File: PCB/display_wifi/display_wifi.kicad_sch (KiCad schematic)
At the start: 17 parts, among them J1 Conn_01x02, J2 Conn_01x10, SW1 SW_Push, SW2 SW_Push, SW3 SW_Push, U1 NINA-W132, U2 OPT4001DNPRQ1

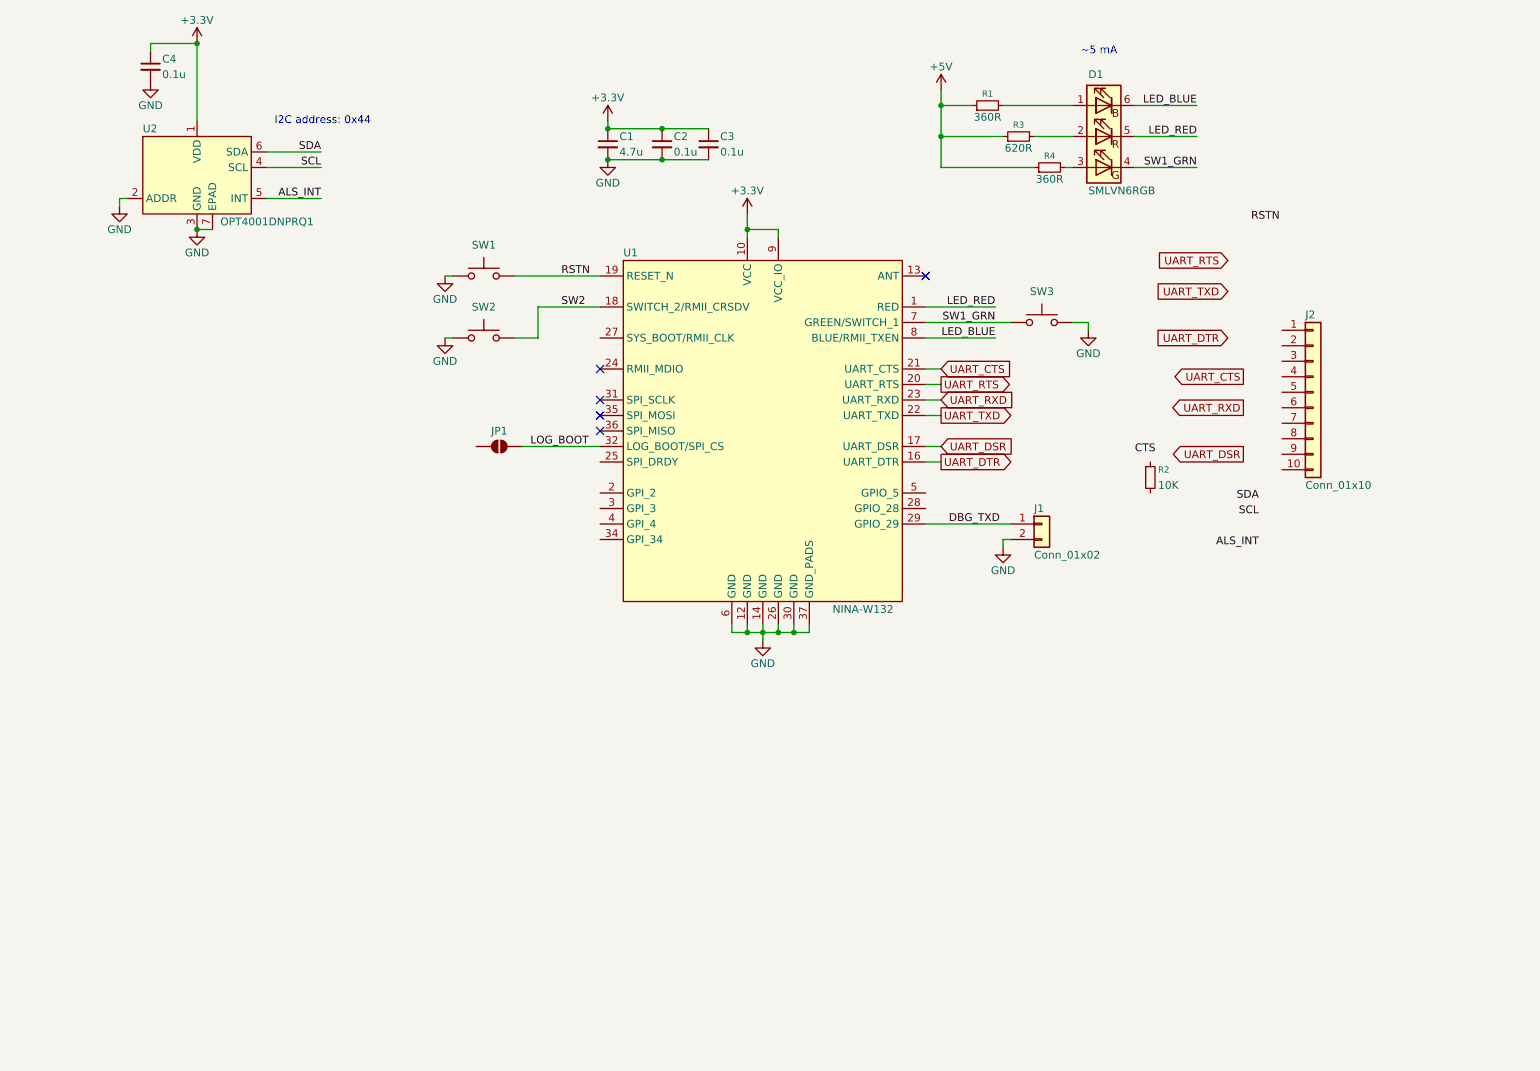
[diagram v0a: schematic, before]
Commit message: Added light sensor, IR remote sensor, test connectors, and routed PCB for display
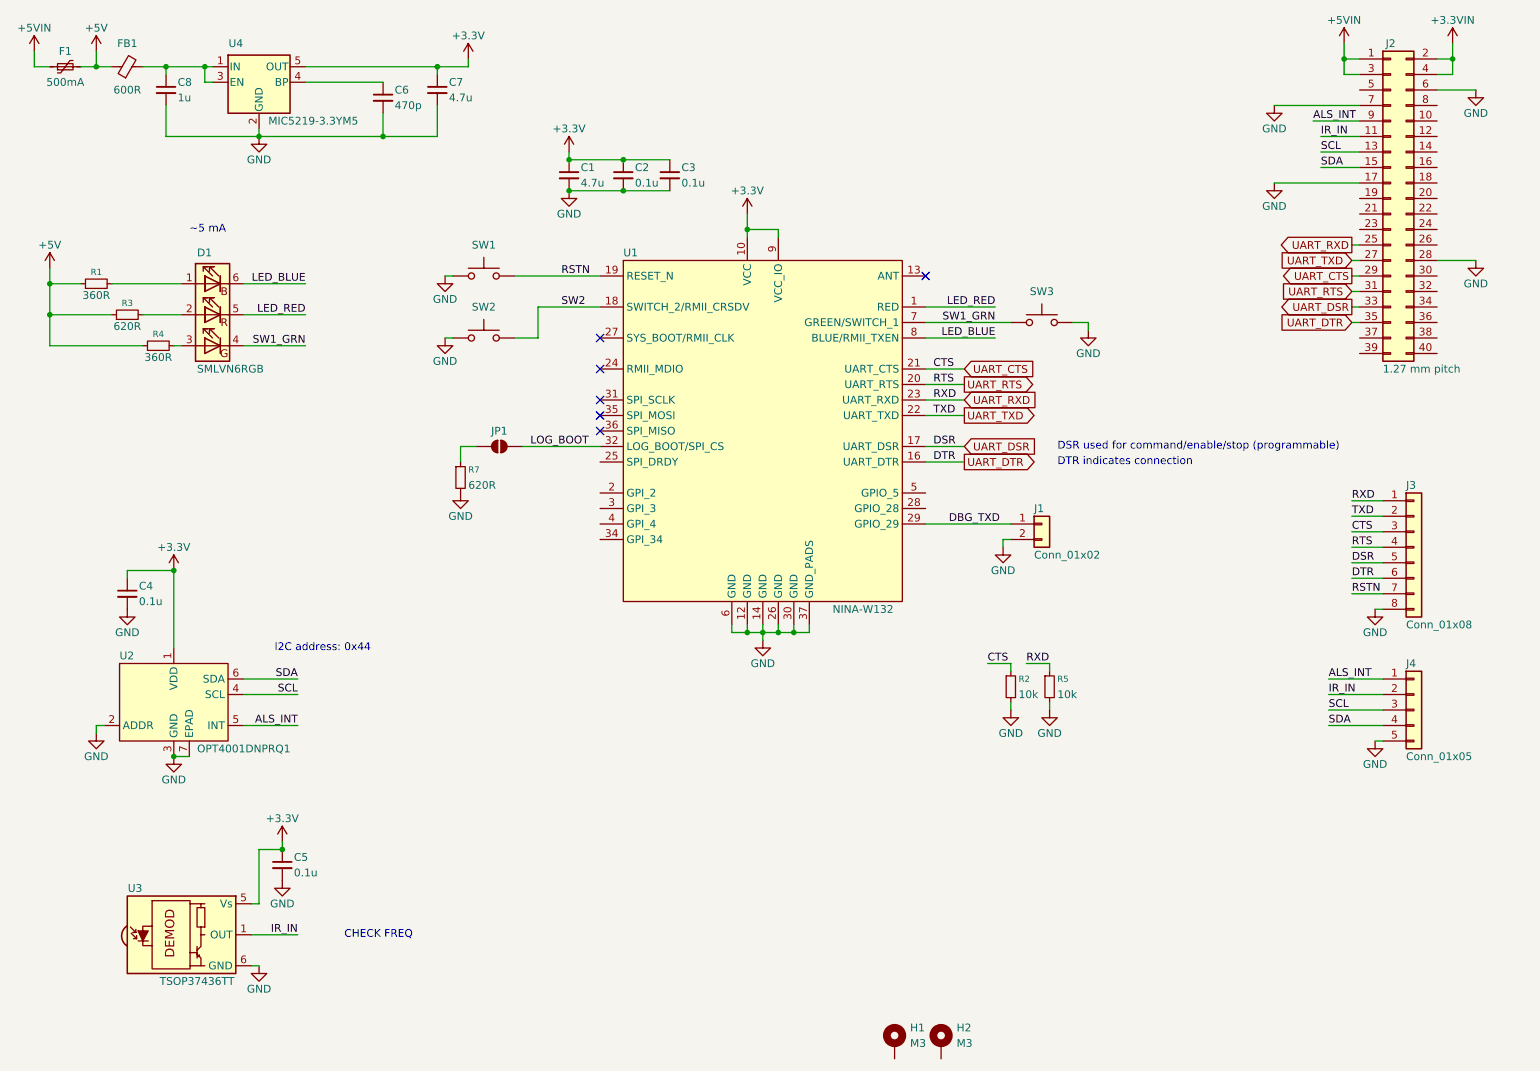
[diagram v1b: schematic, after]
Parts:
- removed J2: Conn_01x10, Connector_PinSocket_2.54mm:PinSocket_1x10_P2.54mm_Vertical, symbol Connector_Generic:Conn_01x10
- added C5: 0.1u, Capacitor_SMD:C_0402_1005Metric, symbol Device:C_Small
- added C6: 470p, Capacitor_SMD:C_0402_1005Metric, symbol Device:C_Small
- added C7: 4.7u, Capacitor_SMD:C_0603_1608Metric, symbol Device:C_Small
- added C8: 1u, Capacitor_SMD:C_0402_1005Metric, symbol Device:C_Small
- added F1: 500mA, Fuse:Fuse_1206_3216Metric, symbol Device:Polyfuse_Small
- added FB1: 600R, Inductor_SMD:L_0805_2012Metric, symbol Device:FerriteBead_Small
- added H1, H2: M3, MountingHole:MountingHole_3.2mm_M3_Pad, symbol Mechanical:MountingHole_Pad
- added J2: 1.27 mm pitch, Connector_PinSocket_1.27mm:PinSocket_2x20_P1.27mm_Vertical, symbol Connector_Generic:Conn_02x20_Odd_Even
- added J3: Conn_01x08, Connector_PinHeader_2.54mm:PinHeader_1x08_P2.54mm_Vertical, symbol Connector_Generic:Conn_01x08
- added J4: Conn_01x05, Connector_PinHeader_2.54mm:PinHeader_1x05_P2.54mm_Vertical, symbol Connector_Generic:Conn_01x05
- added R5: 10k, Resistor_SMD:R_0603_1608Metric, symbol Device:R_Small
- added R7: 620R, Resistor_SMD:R_0603_1608Metric, symbol Device:R_Small
- added U3: TSOP37436TT, DWlib:Vishay_BELOBOG-4Pin, symbol DWlib:TSOP374xx
- added U4: MIC5219-3.3YM5, Package_TO_SOT_SMD:SOT-23-5, symbol Regulator_Linear:MIC5219-3.3YM5
- D1: MPN (none) -> SMLVN6RGB7W1; Mouser PN (none) -> 755-SMLVN6RGB7W1
- J1: footprint Connector_PinSocket_2.54mm:PinSocket_1x02_P2.54mm_Vertical -> Connector_PinHeader_2.54mm:PinHeader_1x02_P2.54mm_Vertical; now left out of the parts list
- R2: value 10K -> 10k
- SW1, SW2, SW3: value SW_Push -> TL3305; MPN (none) -> TL3305BF100QG; Mouser PN (none) -> 612-TL3305BF100QG
- U2: MPN (none) -> OPT4001DNPRQ1; Mouser PN (none) -> 595-OPT4001DNPRQ1
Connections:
- net +3.3V: now also C5.1, C7.1, U3.5 (Vs), U4.5 (OUT)
- net +5V: now also F1.2, FB1.1
- net ALS_INT: now also J2.9 (Pin_9), J4.1 (Pin_1)
- net GND: now also R2.2, C5.2, C6.2, C7.2, C8.2, J2.17 (Pin_17), J2.28 (Pin_28), J2.6 (Pin_6), J2.7 (Pin_7), J3.8 (Pin_8), J4.5 (Pin_5), R5.2, R7.2, U3.6 (GND), U3.8 (GND), U4.2 (GND)
- net RSTN: now also J3.7 (Pin_7)
- net SCL: now also J2.13 (Pin_13), J4.3 (Pin_3)
- net SDA: now also J2.15 (Pin_15), J4.4 (Pin_4)
- net UART_CTS: now also R2.1, J2.29 (Pin_29), J3.3 (Pin_3)
- net UART_DSR: now also J2.33 (Pin_33), J3.5 (Pin_5)
- net UART_DTR: now also J2.35 (Pin_35), J3.6 (Pin_6)
- net UART_RTS: now also J2.31 (Pin_31), J3.4 (Pin_4)
- net UART_RXD: now also J2.25 (Pin_25), J3.1 (Pin_1), R5.1
- net UART_TXD: now also J2.27 (Pin_27), J3.2 (Pin_2)
- net at JP1.1 (A): now also R7.1
- new net: C6.1, U4.4 (BP)
- new net: C8.1, FB1.2, U4.1 (IN), U4.3 (EN)
- new net +3.3VIN: J2.2 (Pin_2), J2.4 (Pin_4)
- new net +5VIN: F1.1, J2.1 (Pin_1), J2.3 (Pin_3)
- new net IR_IN: J2.11 (Pin_11), J4.2 (Pin_2), U3.1 (OUT)
- no-connect marks 5 -> 6
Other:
- note added: "CHECK FREQ"
- note added: "DSR used for command/enable/stop (programmable)"
- note added: "DTR indicates connection"
- moved on the sheet: C1, C2, C3, C4, D1, R1, R2, R3, R4, U2

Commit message: Added passthrough for power and SWD to simplify connections. Added part numbers.
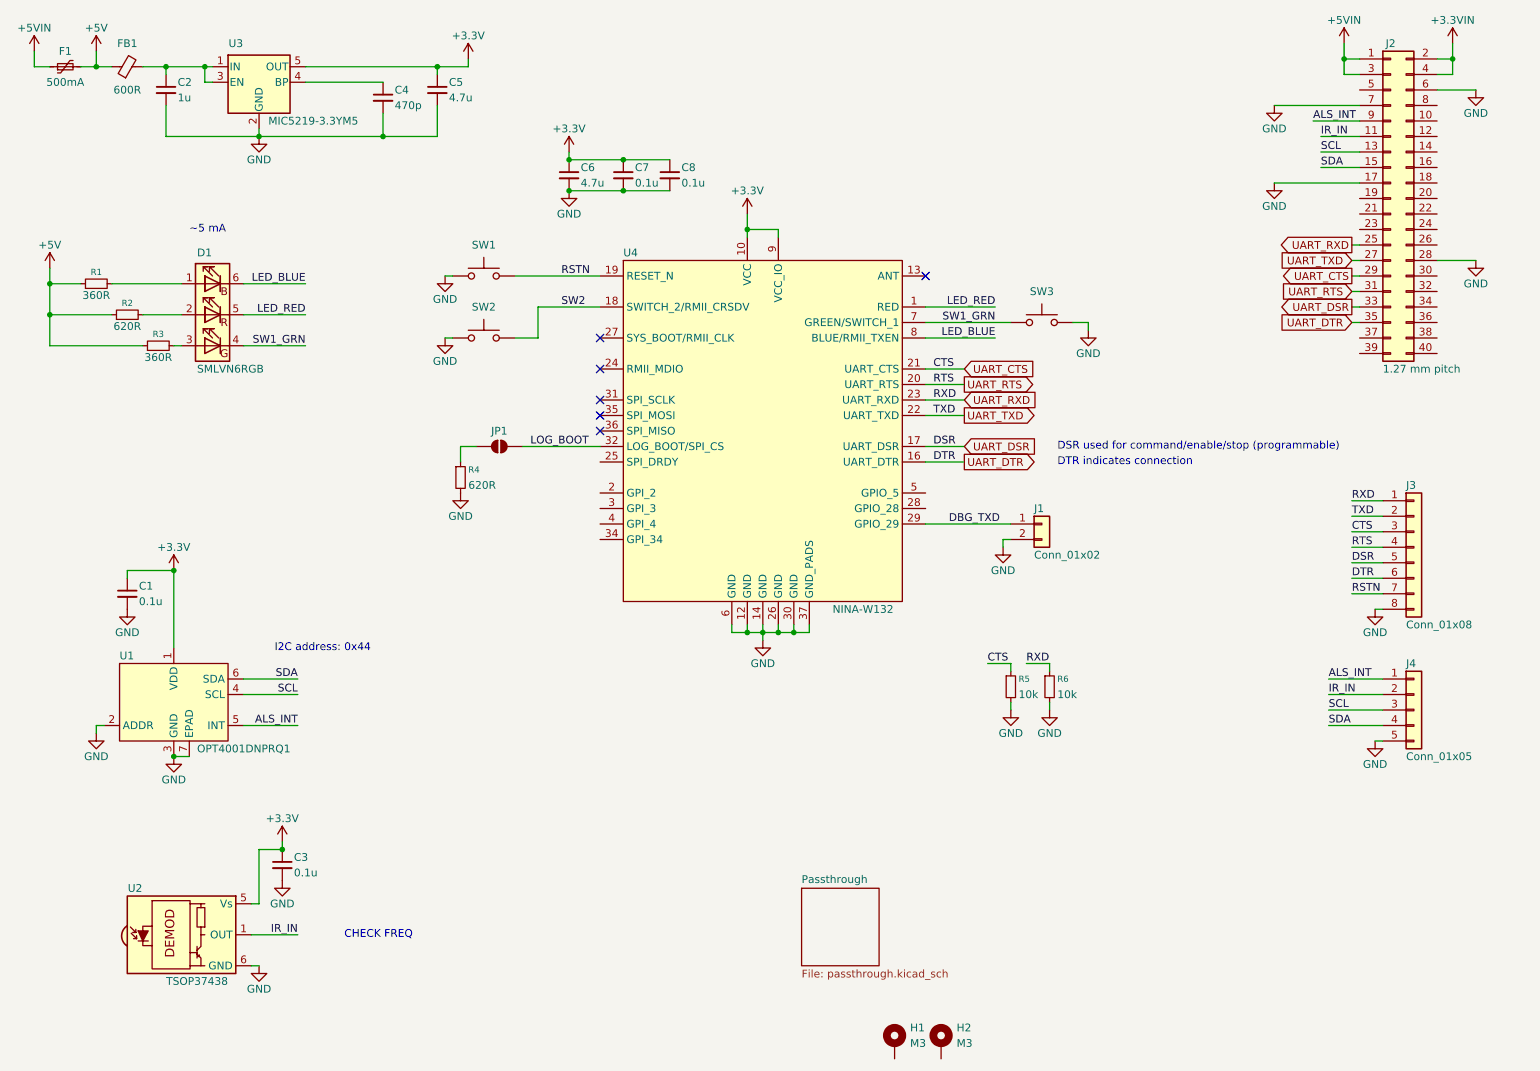
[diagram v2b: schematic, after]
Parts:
- C1: renamed from C4; MPN (none) -> CL05B104KA5NNNC; Mouser PN (none) -> 187-CL05B104KA5NNNC
- C2: renamed from C8; MPN (none) -> CL05A105KA5NQNC; Mouser PN (none) -> 187-CL05A105KA5NQNC
- C3: renamed from C5; MPN (none) -> CL05B104KA5NNNC; Mouser PN (none) -> 187-CL05B104KA5NNNC
- C4: renamed from C6; MPN (none) -> GRM1555C2A471JE01D; Mouser PN (none) -> 81-GRM1555C2A471JE1D
- C5: renamed from C7; MPN (none) -> CL10A475KO8NNNC; Mouser PN (none) -> 187-CL10A475KO8NNNC
- C6: renamed from C1; MPN (none) -> CL10A475KO8NNNC; Mouser PN (none) -> 187-CL10A475KO8NNNC
- C7: renamed from C2; MPN (none) -> CL05B104KA5NNNC; Mouser PN (none) -> 187-CL05B104KA5NNNC
- C8: renamed from C3; MPN (none) -> CL05B104KA5NNNC; Mouser PN (none) -> 187-CL05B104KA5NNNC
- FB1: MPN (none) -> BLM21SP601SZ1D; Mouser PN (none) -> 81-BLM21SP601SZ1D
- J3, J4: now left out of the parts list
- U2: renamed from U3; value TSOP37436TT -> TSOP37438; MPN TSOP37436TT1 -> TSOP37438TT1; Mouser PN (none) -> 78-TSOP37438TT1
- renumbered R3 to R2, R4 to R3, R7 to R4, R2 to R5, R5 to R6, U2 to U1, U4 to U3, U1 to U4
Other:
- added sheet Passthrough (passthrough.kicad_sch)

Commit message: Updated PCB to v1.1
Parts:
- added C9: 22u, Capacitor_SMD:C_1210_3225Metric, symbol Device:C_Small
- added R7, R8: 1.2k, Resistor_SMD:R_0603_1608Metric, symbol Device:R_Small
- added R9: 10k, Resistor_SMD:R_0603_1608Metric, symbol Device:R_Small
- R1, R3: value 360R -> 1.8k
- R2: value 620R -> 3.3k
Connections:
- net +3.3V: now also C9.1, R7.1, R8.1, R9.1
- net ALS_INT: now also R9.2
- net GND: now also C9.2
- net SCL: now also R8.2
- net SDA: now also R7.2
- net UART_DSR: now also J2.35 (Pin_35); no longer J2.33 (Pin_33)
- net UART_DTR: now also J2.36 (Pin_36); no longer J2.35 (Pin_35)
- net DEBUG_TXD: now reaches J2.23 (Pin_23)
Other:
- note added: "FIXES"
- note added: "~1 mA"
- note removed: "CHECK FREQ"
- note removed: "~5 mA"
